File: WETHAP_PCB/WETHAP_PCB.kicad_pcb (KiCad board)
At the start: 2 copper layers, 49 x 85 mm, 11 parts, among them J1 Conn_01x20_Socket, J2 Conn_01x20_Socket

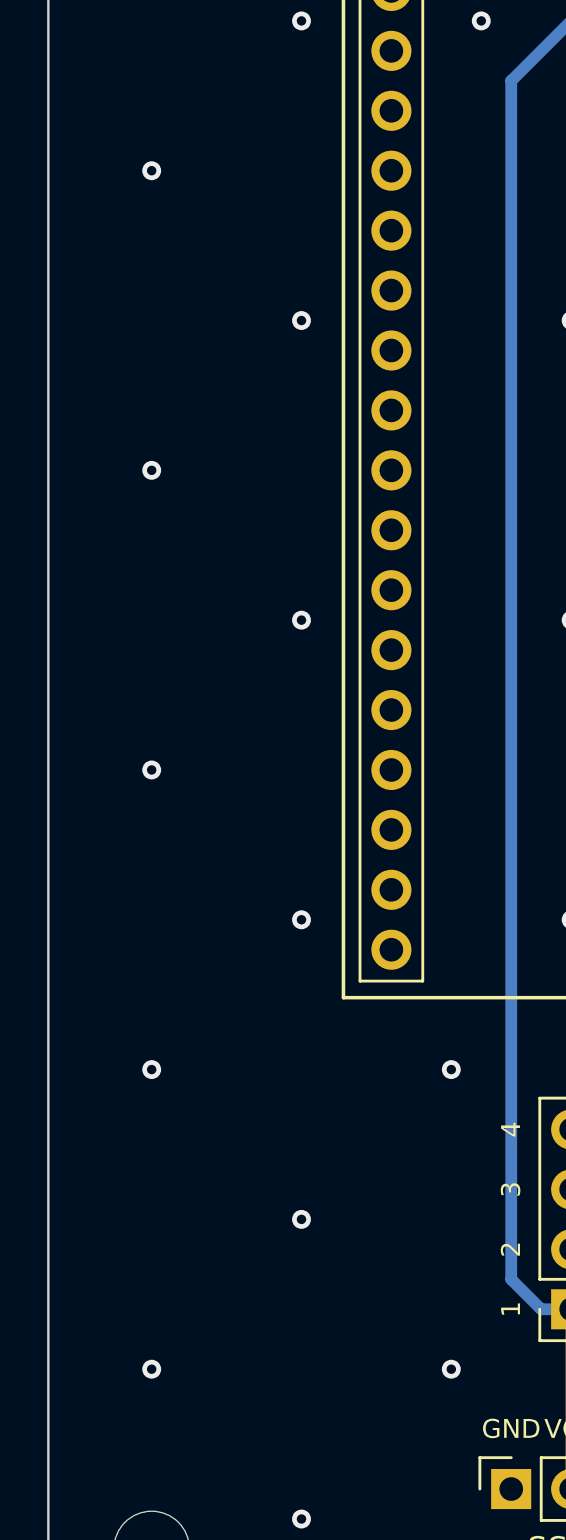
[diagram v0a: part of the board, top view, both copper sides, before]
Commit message: add logo
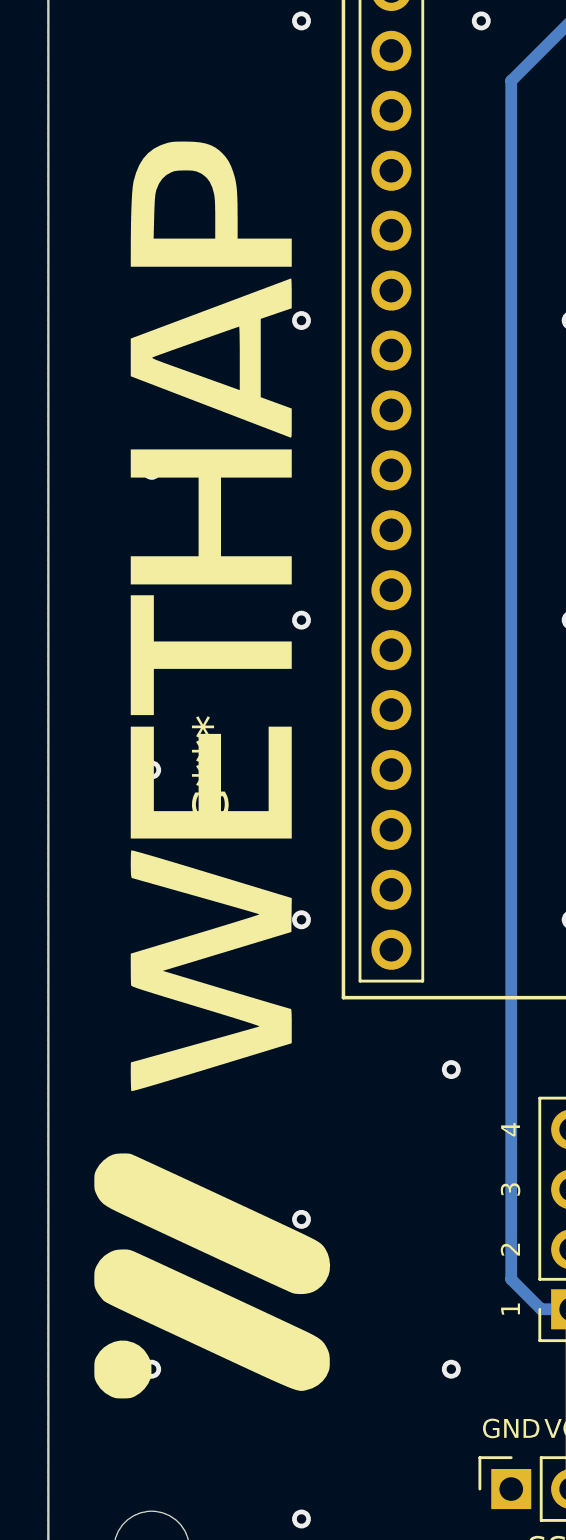
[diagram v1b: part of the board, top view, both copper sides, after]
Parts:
- added G***: LOGO, WETHAP_PCB:WETHAP_logo, F.Cu at (121.9, 106.7)

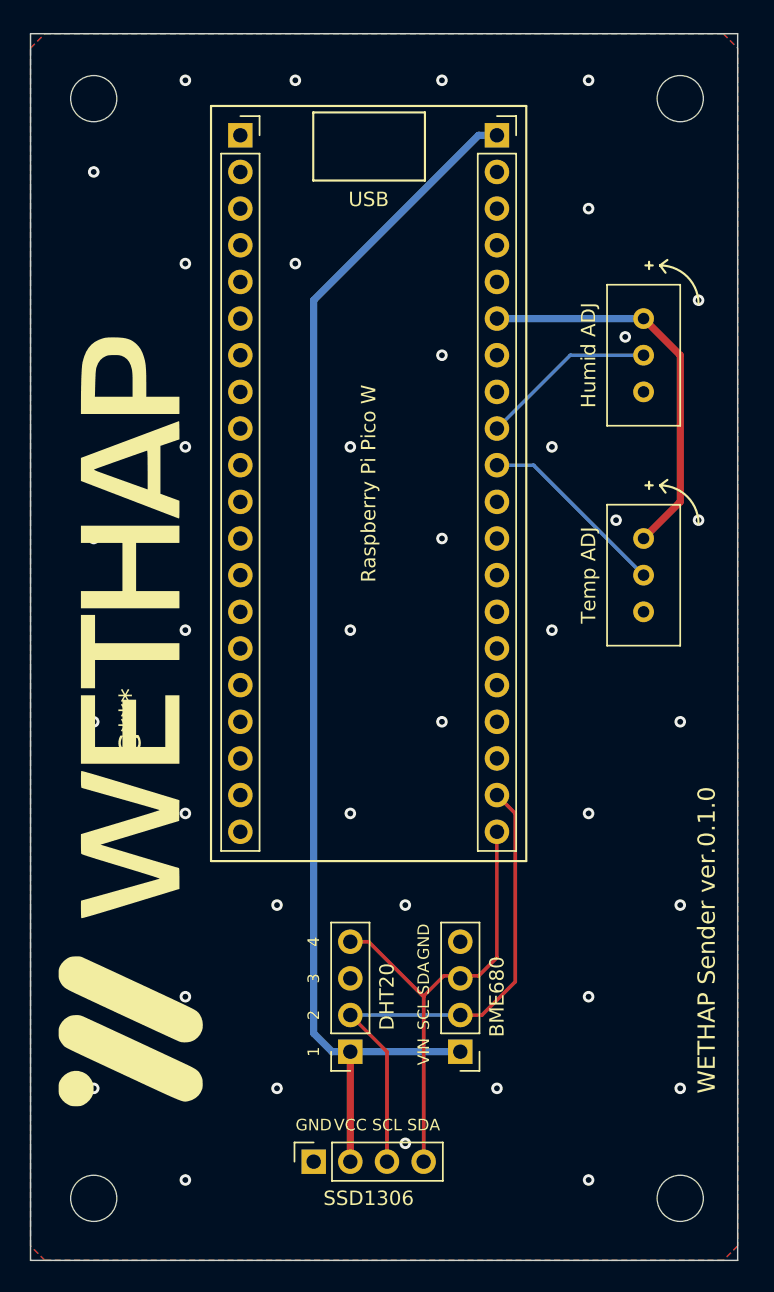
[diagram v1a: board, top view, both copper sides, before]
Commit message: update sender logo
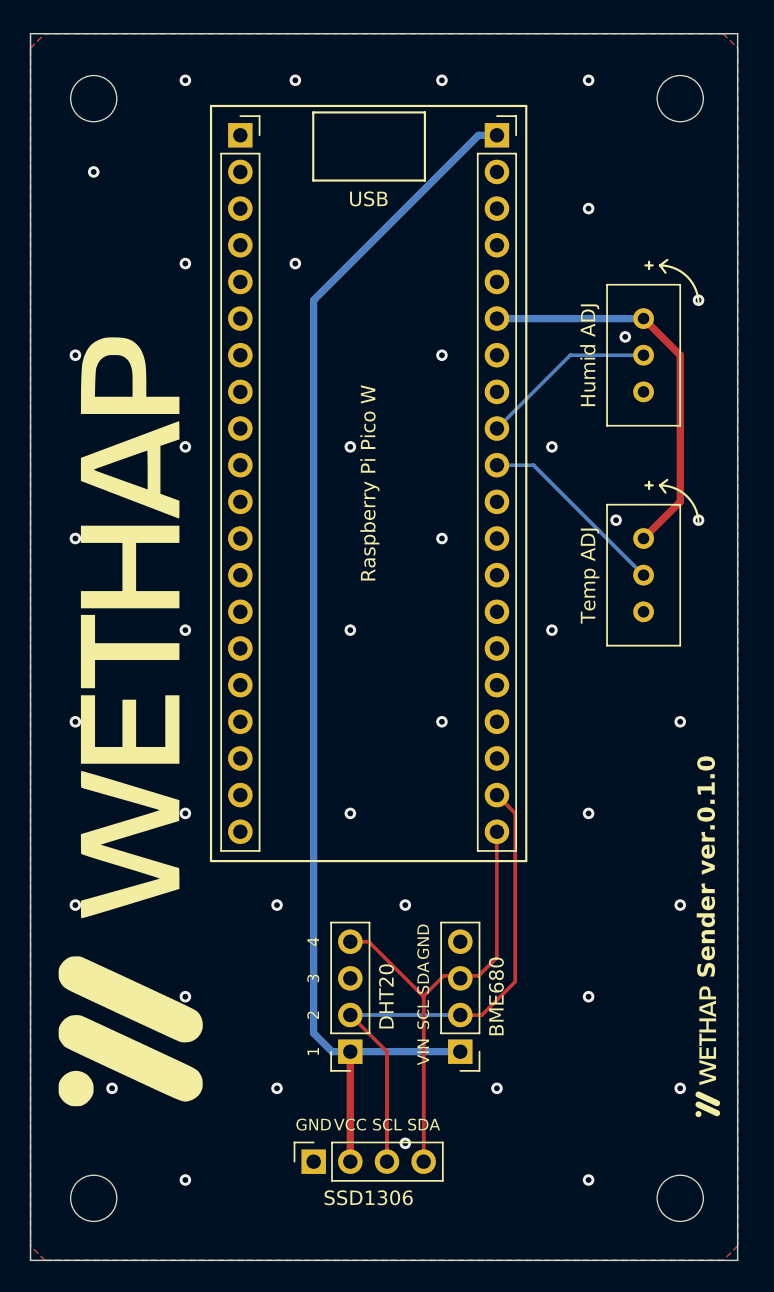
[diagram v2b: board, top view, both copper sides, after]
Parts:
- added G1: LOGO, RPi_Pico:logo, F.Cu at (161.9, 129.5)
- renumbered G*** to G0
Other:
- board text added: "Sender ver.0.1.0"
- board text removed: "WETHAP Sender ver.0.1.0"

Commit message: pcb v0.2.0
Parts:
- removed BME680: Conn_01x04_Socket, Connector_PinHeader_2.54mm:PinHeader_1x04_P2.54mm_Vertical
- added LPS25HB1: Conn_01x04_Socket, Connector_PinSocket_2.54mm:PinSocket_1x04_P2.54mm_Vertical, F.Cu at (130.9, 121.9)
- added LPS25HB2: Conn_01x04_Socket, Connector_PinSocket_2.54mm:PinSocket_1x04_P2.54mm_Vertical, F.Cu at (138.5, 129.5)
- moved DHT20 10.2 mm to (147.3, 129.5)
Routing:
- net sda: track 33.2 -> 45.2 mm
- net vbus: track 86.5 -> 92.5 mm
- net scl: track 37.1 -> 42.7 mm
- net gnd: vias 41 -> 42
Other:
- board text added: "5"
- board text added: "6"
- board text added: "7"
- board text added: "8"
- board text added: "LPS25HB"
- board text added: "Sender ver.0.2.0"
- board text removed: "BME680"
- board text removed: "Sender ver.0.1.0"
- board text removed: "VIN"

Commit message: fix circuit
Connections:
- DHT20 pad 2: scl -> sda
- DHT20 pad 4: sda -> scl
- LPS25HB1 pad 1: gnd -> vbus
- LPS25HB1 pad 2: sda -> scl
- LPS25HB1 pad 3: scl -> sda
- LPS25HB1 pad 4: vbus -> gnd
- LPS25HB2 pad 1: gnd -> (no net)
- LPS25HB2 pad 2: unconnected-(LPS25HB2-Pin_2-Pad2) -> (no net)
- LPS25HB2 pad 3: unconnected-(LPS25HB2-Pin_3-Pad3) -> (no net)
- LPS25HB2 pad 4: vbus -> (no net)
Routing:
- net vbus: track 92.5 -> 100.1 mm
- net sda: track 45.2 -> 41.0 mm
- net scl: track 42.7 -> 45.2 mm
- net gnd: vias 42 -> 43
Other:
- board size 49 x 85 mm -> 49.5 x 85.1 mm
- board text removed: "6"
- board text removed: "7"

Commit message: websocket
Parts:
- removed REF1, REF2, REF3, REF4: MountingHole_3.2mm_M3, MountingHole:MountingHole_3.2mm_M3
- added H1: MountingHole_Pad, MountingHole:MountingHole_3.2mm_M3_DIN965_Pad, F.Cu at (119.4, 63.5)
- added H2: MountingHole_Pad, MountingHole:MountingHole_3.2mm_M3_DIN965_Pad, F.Cu at (160.0, 63.5)
- added H3: MountingHole_Pad, MountingHole:MountingHole_3.2mm_M3_DIN965_Pad, F.Cu at (119.4, 139.7)
- added H4: MountingHole_Pad, MountingHole:MountingHole_3.2mm_M3_DIN965_Pad, F.Cu at (160.0, 139.7)
- moved J2 48.3 mm to (147.3, 114.3), turned to 180 degrees
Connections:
- J2 pad 1: vbus -> sda
- J2 pad 10: Net-(J2-Pin_10) -> unconnected-(J2-Pin_10-Pad10)
- J2 pad 11: unconnected-(J2-Pin_11-Pad11) -> ADC0
- J2 pad 12: unconnected-(J2-Pin_12-Pad12) -> ADC1
- J2 pad 15: unconnected-(J2-Pin_15-Pad15) -> adc_vref
- J2 pad 19: scl -> unconnected-(J2-Pin_19-Pad19)
- J2 pad 2: unconnected-(J2-Pin_2-Pad2) -> scl
- J2 pad 20: sda -> vbus
- J2 pad 6: adc_vref -> unconnected-(J2-Pin_6-Pad6)
- J2 pad 9: Net-(J2-Pin_9) -> unconnected-(J2-Pin_9-Pad9)
- RV1 pad 1: adc_vref -> gnd
- RV1 pad 2: Net-(J2-Pin_10) -> ADC0
- RV1 pad 3: gnd -> adc_vref
- RV2 pad 1: adc_vref -> gnd
- RV2 pad 2: Net-(J2-Pin_9) -> ADC1
- RV2 pad 3: gnd -> adc_vref
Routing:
- net Net-(J2-Pin_10): track 13.3 -> 0.00 mm
- net ADC0: track 0.00 -> 13.3 mm
- net Net-(J2-Pin_9): track 12.3 -> 0.00 mm
- net ADC1: track 0.00 -> 12.3 mm
- net vbus: track 100.1 -> 93.1 mm
- net scl: track 45.2 -> 51.0 mm
- net sda: track 41.0 -> 42.9 mm
- net adc_vref: track 27.5 -> 29.3 mm
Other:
- board text added: "Sender ver.0.3.0"
- board text removed: "Sender ver.0.2.0"

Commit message: fix pcb
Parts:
- moved LPS25HB2 0.09 mm to (138.4, 129.5)
- moved LPS25HB1 0.07 mm to (130.8, 121.9)
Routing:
- net vbus: track 93.1 -> 99.2 mm
- net sda: track 42.9 -> 42.2 mm
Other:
- board text added: "Sender ver.0.3.2"
- board text removed: "Sender ver.0.3.0"
